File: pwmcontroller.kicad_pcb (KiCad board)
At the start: 2 copper layers, 46.2 x 53.8 mm, 19 parts, among them J1 CONN_01X04, J2 CONN_01X04, U1 WPMIx9200501S, U2 NE555

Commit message: Fix component values
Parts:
- R1: value 100K -> 1K
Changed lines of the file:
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@@
   )
   (setup
-    (last_trace_width 0.5)
+    (last_trace_width 0.25)
     (user_trace_width 0.25)
     (user_trace_width 0.5)
@@
       (effects (font (size 1 1) (thickness 0.15)))
     )
-    (fp_text value 100K (at 5.08 2.31 270) (layer F.Fab)
+    (fp_text value 1K (at 5.08 2.31 270) (layer F.Fab)
       (effects (font (size 1 1) (thickness 0.15)))
     )
@@
   (segment (start 150.114 89.408) (end 147.574 89.408) (width 1.5) (layer F.Cu) (net 10))
   (segment (start 152.52 91.814) (end 150.114 89.408) (width 1.5) (layer F.Cu) (net 10))
-  (segment (start 160.274 93.98) (end 160.274 91.948) (width 0.5) (layer B.Cu) (net 11) (status 400000))
-  (segment (start 149.98 92.082) (end 149.98 94) (width 0.5) (layer B.Cu) (net 11) (status 800000))
+  (segment (start 160.274 93.98) (end 160.274 91.948) (width 0.5) (layer B.Cu) (net 11))
+  (segment (start 149.98 92.082) (end 149.98 94) (width 0.5) (layer B.Cu) (net 11))
   (segment (start 150.876 91.186) (end 149.98 92.082) (width 0.5) (layer B.Cu) (net 11))
   (segment (start 152.794 91.186) (end 150.876 91.186) (width 0.5) (layer B.Cu) (net 11))

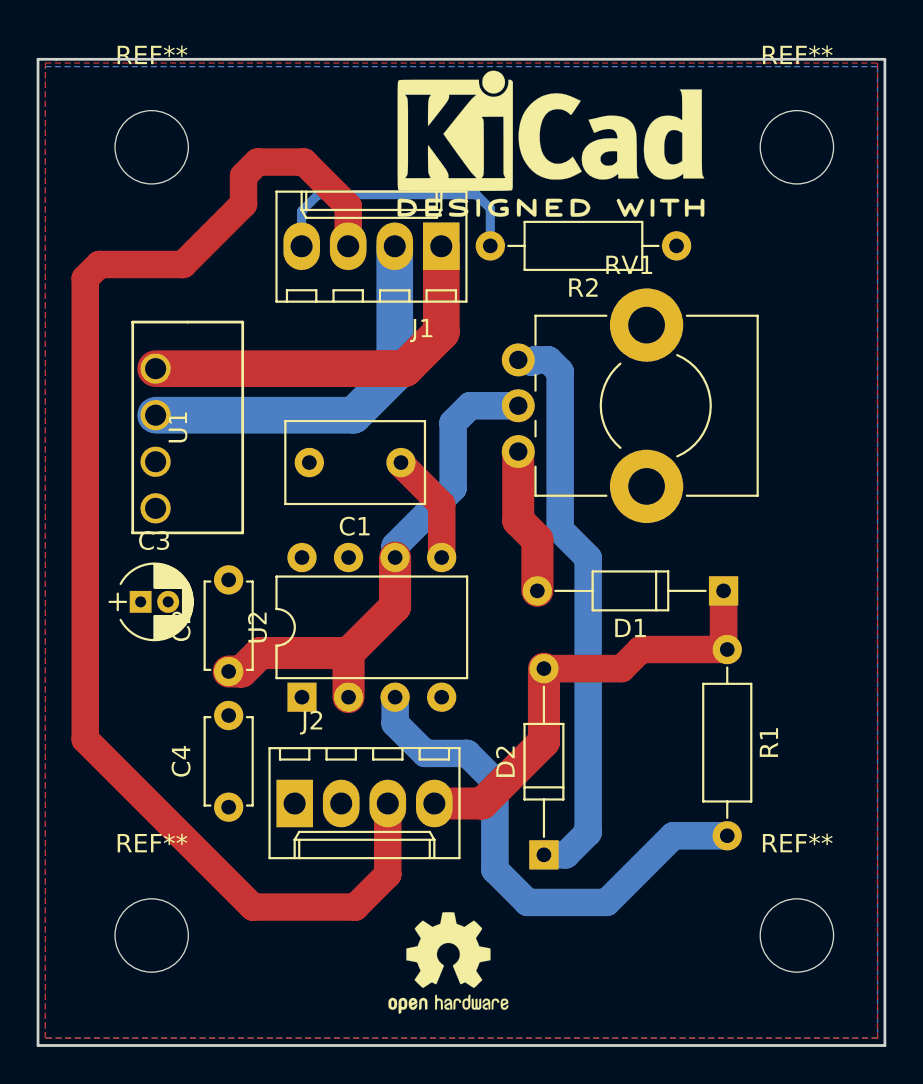
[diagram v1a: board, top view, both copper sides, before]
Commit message: Remove mounting hole silkscreen label
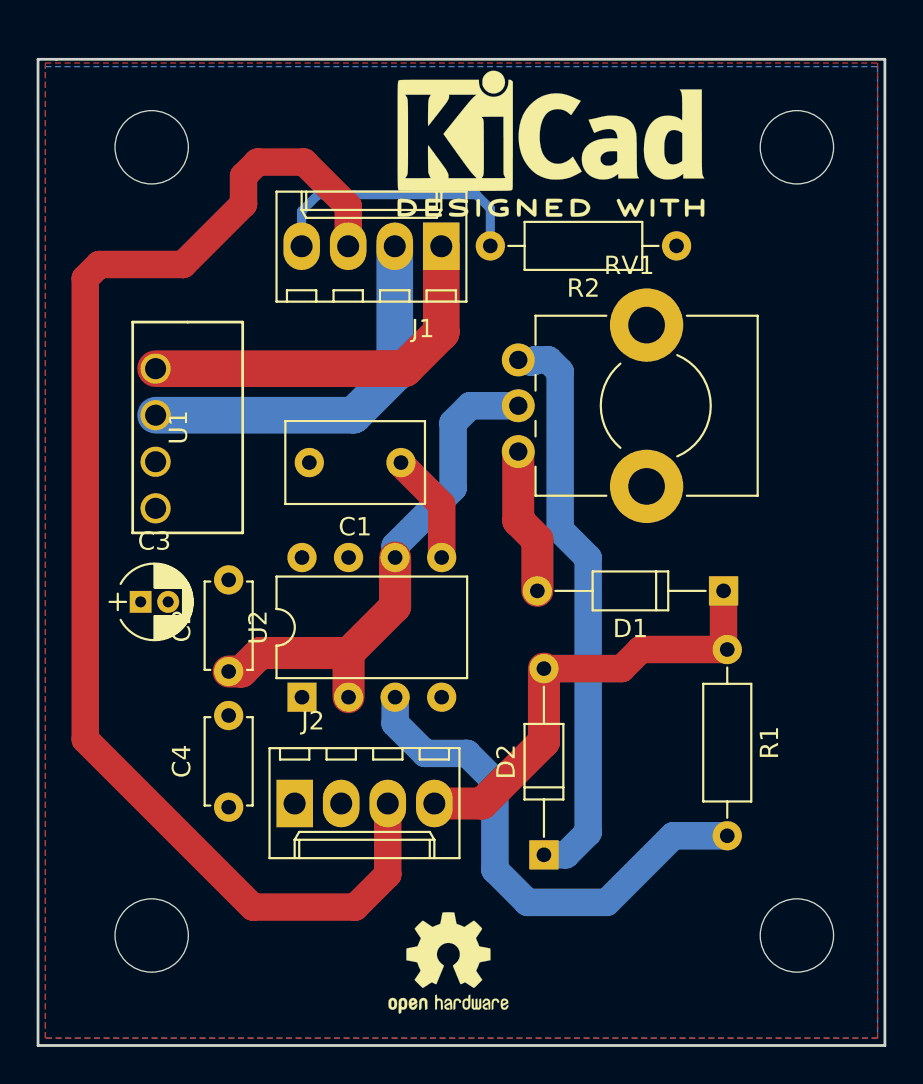
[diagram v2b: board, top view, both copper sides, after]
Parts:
- renumbered REF** to ?
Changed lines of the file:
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@@
     (links 26)
     (no_connects 0)
-    (area 135.524999 83.724999 181.875001 137.675001)
+    (area 134.385714 82.625 184.414286 137.675001)
     (thickness 1.6)
     (drawings 5)
@@
   (page A4)
   (layers
-    (0 F.Cu signal hide)
-    (31 B.Cu signal)
+    (0 F.Cu signal)
+    (31 B.Cu signal hide)
     (32 B.Adhes user)
     (33 F.Adhes user)
@@
     (descr "Mounting Hole 4mm, no annular")
     (tags "mounting hole 4mm no annular")
-    (fp_text reference REF** (at 0 -5) (layer F.SilkS)
+    (fp_text reference "" (at 0 -5) (layer F.SilkS)
       (effects (font (size 1 1) (thickness 0.15)))
     )
@@
     (descr "Mounting Hole 4mm, no annular")
     (tags "mounting hole 4mm no annular")
-    (fp_text reference REF** (at 0 -5) (layer F.SilkS)
+    (fp_text reference "" (at 0 -5) (layer F.SilkS)
       (effects (font (size 1 1) (thickness 0.15)))
     )
@@
     (descr "Mounting Hole 4mm, no annular")
     (tags "mounting hole 4mm no annular")
-    (fp_text reference REF** (at 0 -5) (layer F.SilkS)
+    (fp_text reference "" (at 0 -5) (layer F.SilkS)
       (effects (font (size 1 1) (thickness 0.15)))
     )
@@
     (descr "Mounting Hole 4mm, no annular")
     (tags "mounting hole 4mm no annular")
-    (fp_text reference REF** (at 0 -5) (layer F.SilkS)
-      (effects (font (size 1 1) (thickness 0.15)))
-    )
+    (fp_text reference "" (at 0 -5) (layer F.SilkS)
+      (effects (font (size 1 1) (thickness 0.15)))
+    )

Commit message: Shrink PCB to smaller dimensions
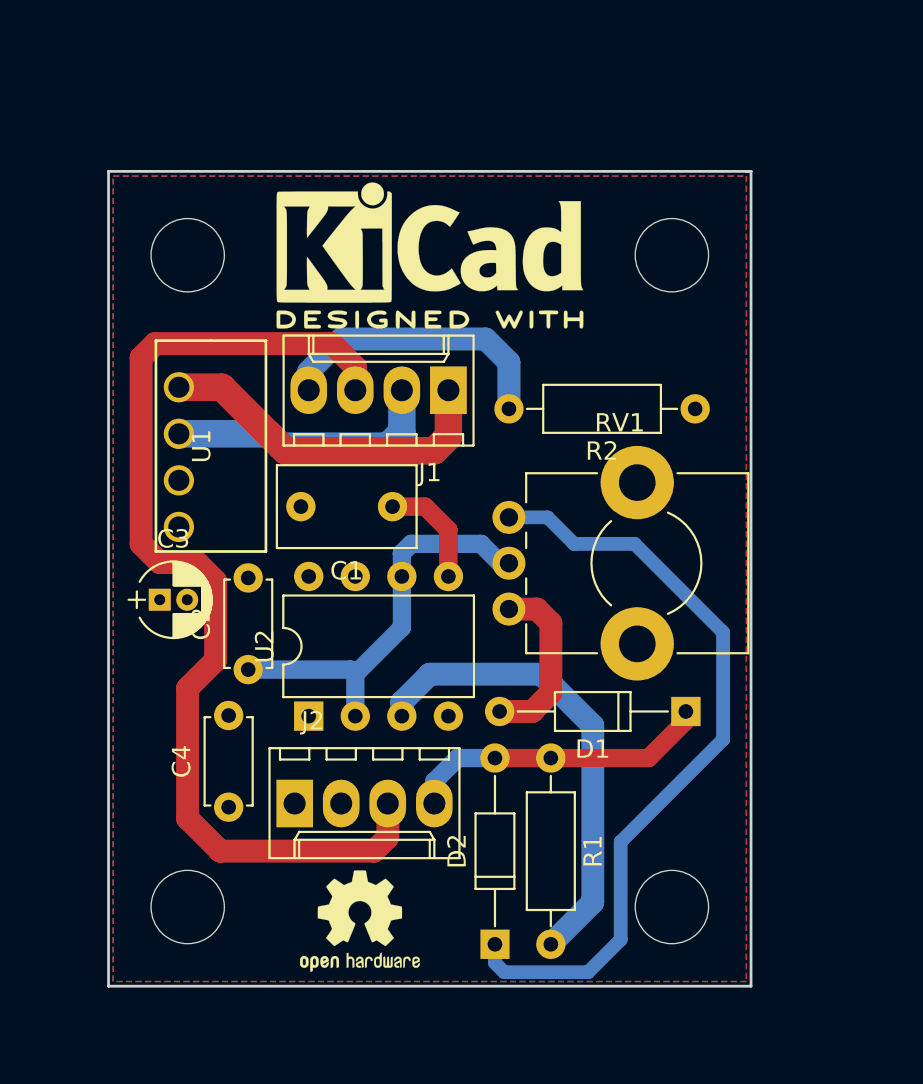
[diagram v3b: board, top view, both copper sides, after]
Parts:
- moved R1 11.3 mm to (163.6, 121.9)
- moved ? 9.01 mm to (170.2, 94.5)
- moved REF*** 8.99 mm to (157.0, 94.5)
- moved R2 8.95 mm to (171.4, 102.9)
- moved RV1 8.61 mm to (161.3, 113.8)
- moved J1 7.86 mm to (158.0, 101.9)
- moved ? 6.99 mm to (170.2, 130.0)
- moved D1 6.89 mm to (170.9, 119.4)
- moved ? 6.21 mm to (143.8, 94.5)
- moved D2 5.56 mm to (160.5, 132.1)
- moved REF*** 5.34 mm to (153.2, 130.8)
- moved ? 2.50 mm to (143.8, 130.0)
- moved C1 2.45 mm to (154.9, 108.2)
- moved U1 1.63 mm to (145.0, 104.9)
- moved U2 1.10 mm to (150.4, 119.6)
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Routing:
- net /FAN_RPM: track 71.1 -> 56.3 mm
- net Net-(D2-Pad1): track 31.3 -> 42.2 mm
- net /PWM_OUT: track 25.1 -> 16.8 mm
- net +12V: track 20.9 -> 15.0 mm
- net /TRIG: track 28.2 -> 22.4 mm
- net GNDS: track 21.1 -> 19.0 mm
- net Net-(R1-Pad2): track 27.9 -> 25.8 mm
- net Net-(D1-Pad2): track 8.03 -> 9.63 mm
- net Net-(J1-Pad4): track 14.9 -> 15.7 mm
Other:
- board size 46.2 x 53.8 mm -> 35.1 x 44.5 mm

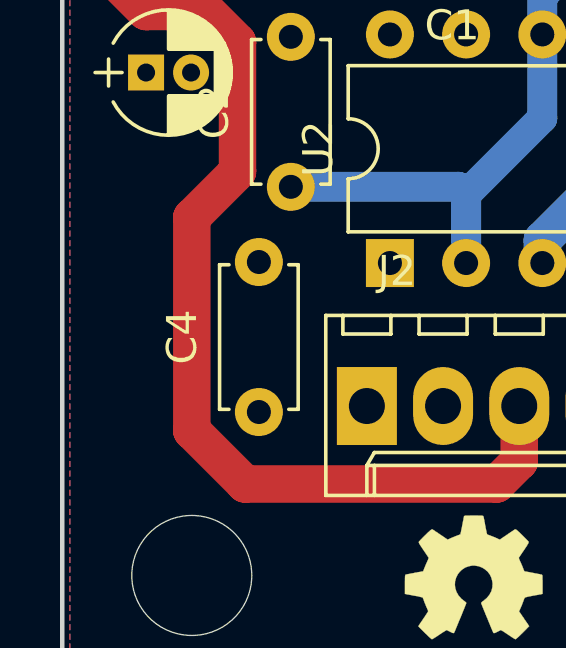
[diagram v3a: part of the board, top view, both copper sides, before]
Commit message: Add Silkscreen description on Board
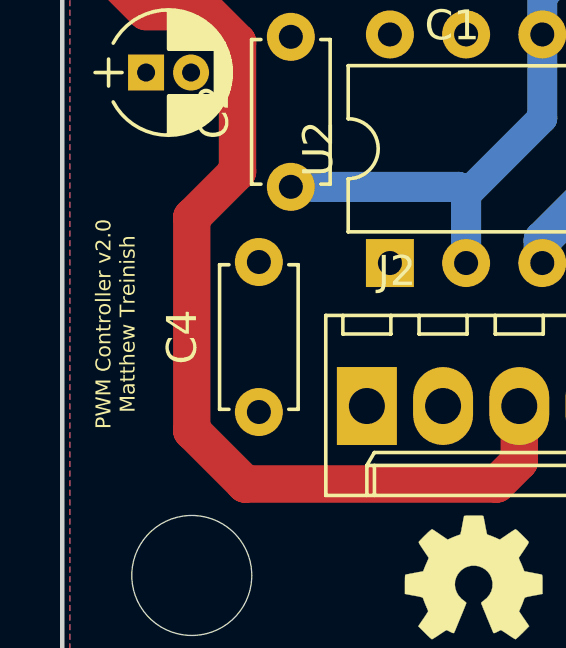
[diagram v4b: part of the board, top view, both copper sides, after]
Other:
- board text added: "PWM Controller v2.0 Matthew Treinish"
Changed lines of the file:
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@@
     (links 26)
     (no_connects 1)
-    (area 136.349714 88.513 177.594286 136.123)
+    (area 139.370999 89.840999 174.573001 134.441001)
     (thickness 1.6)
-    (drawings 5)
+    (drawings 6)
     (tracks 72)
     (zones 0)
@@
     )
   )
+  (gr_text "PWM Controller v2.0\nMatthew Treinish" (at 141.224 121.666 90) (layer F.SilkS)
+    (effects (font (size 0.5 0.5) (thickness 0.125)))
+  )
   (gr_line (start 174.498 89.916) (end 174.244 89.916) (angle 90) (layer Edge.Cuts) (width 0.15))

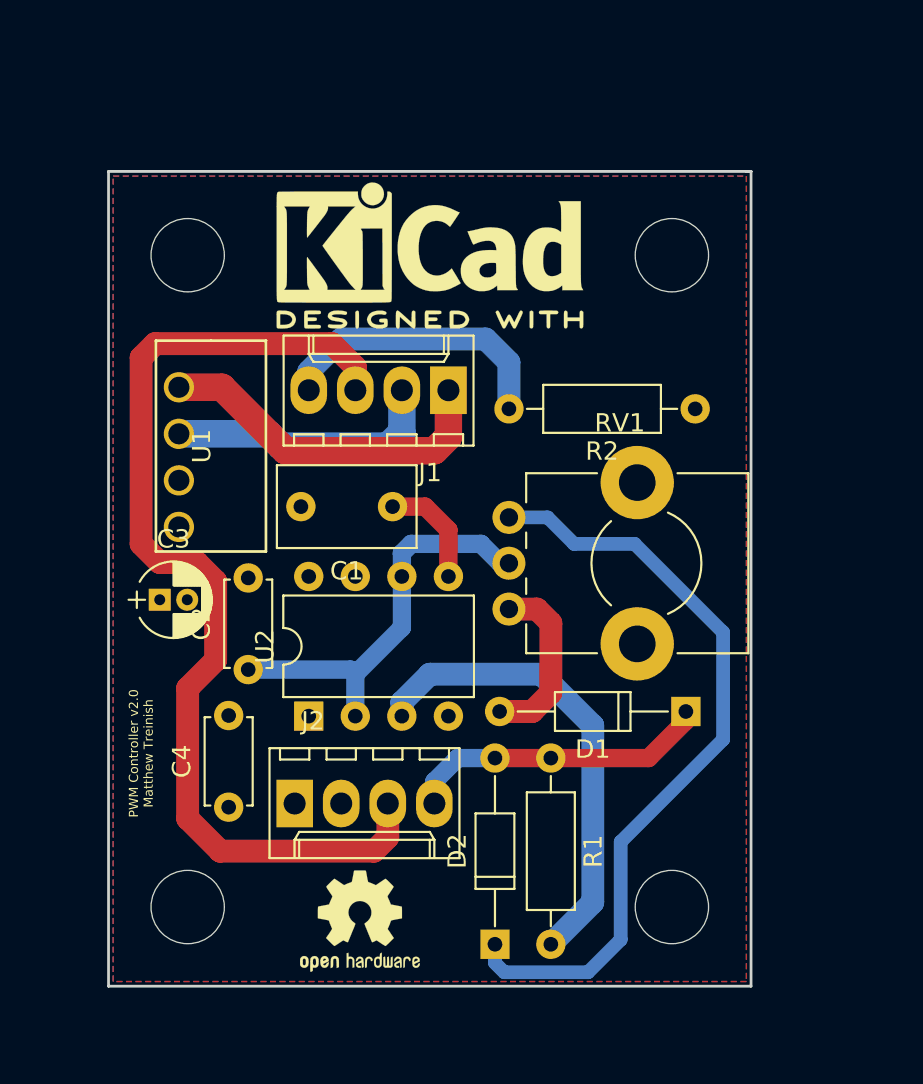
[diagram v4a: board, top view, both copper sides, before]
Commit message: Move mouting holes in slightly
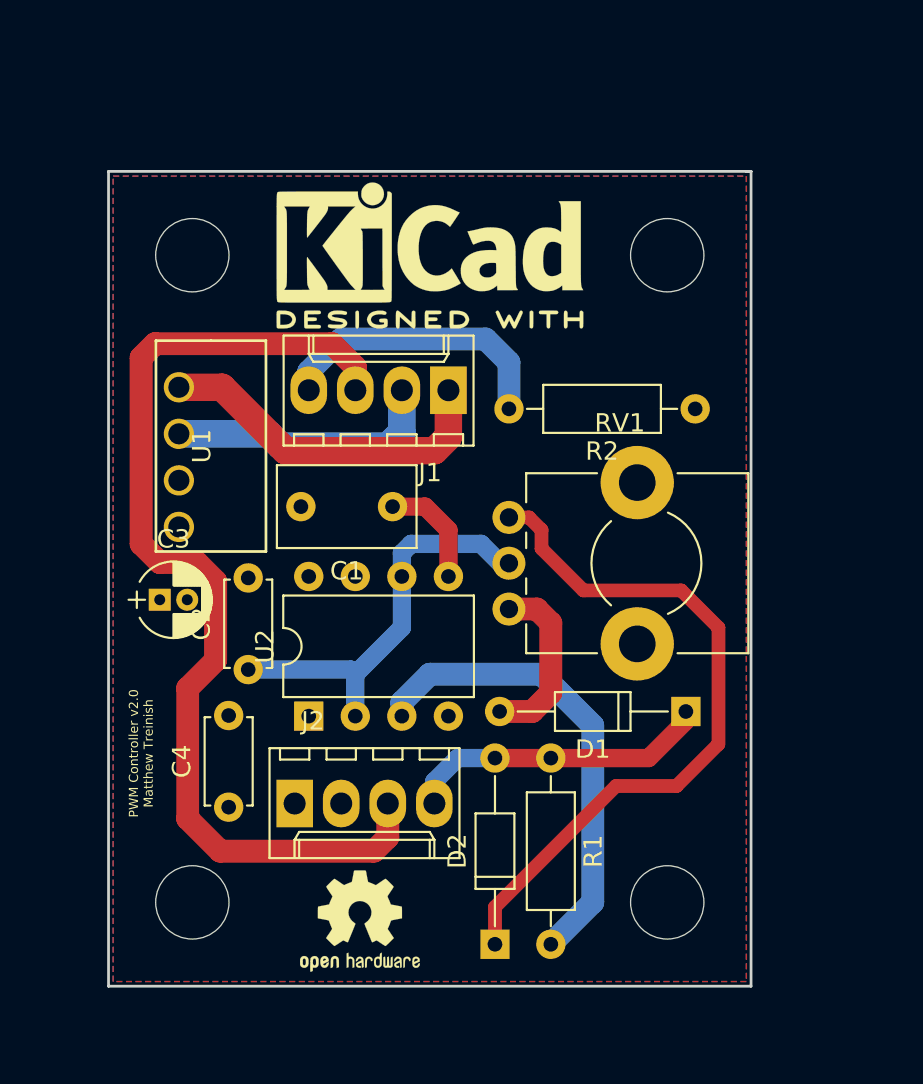
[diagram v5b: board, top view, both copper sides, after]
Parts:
- moved ? 0.36 mm to (169.9, 129.8)
- moved ? 0.36 mm to (144.0, 129.8)
- moved ? 0.25 mm to (169.9, 94.5)
- moved ? 0.25 mm to (144.0, 94.5)
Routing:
- net Net-(D2-Pad1): track 42.2 -> 38.8 mm
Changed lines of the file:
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@@
   )
   (setup
-    (last_trace_width 0.25)
+    (last_trace_width 0.75)
     (user_trace_width 0.25)
     (user_trace_width 0.5)
@@
   )
   (module Mounting_Holes:MountingHole_4mm (layer F.Cu)
-    (at 143.764 130.048)
+    (at 144.018 129.794)
     (descr "Mounting Hole 4mm, no annular")
     (tags "mounting hole 4mm no annular")
@@
   )
   (module Mounting_Holes:MountingHole_4mm (layer F.Cu)
-    (at 170.18 130.048)
+    (at 169.926 129.794)
     (descr "Mounting Hole 4mm, no annular")
     (tags "mounting hole 4mm no annular")
@@
   )
   (module Mounting_Holes:MountingHole_4mm (layer F.Cu)
-    (at 170.18 94.488)
+    (at 169.926 94.488)
     (descr "Mounting Hole 4mm, no annular")
     (tags "mounting hole 4mm no annular")
@@
   )
   (module Mounting_Holes:MountingHole_4mm (layer F.Cu)
-    (at 143.764 94.488)
+    (at 144.018 94.488)
     (descr "Mounting Hole 4mm, no annular")
     (tags "mounting hole 4mm no annular")
@@
   (segment (start 163.576 118.364) (end 163.576 114.554) (width 1.25) (layer F.Cu) (net 6))
   (segment (start 162.56 119.38) (end 163.576 118.364) (width 1.25) (layer F.Cu) (net 6))
-  (segment (start 160.528 132.08) (end 160.528 133.096) (width 0.75) (layer B.Cu) (net 7))
-  (segment (start 163.402 108.792) (end 161.29 108.792) (width 0.75) (layer B.Cu) (net 7))
-  (segment (start 164.846 110.236) (end 163.402 108.792) (width 0.75) (layer B.Cu) (net 7))
-  (segment (start 168.148 110.236) (end 164.846 110.236) (width 0.75) (layer B.Cu) (net 7))
-  (segment (start 172.974 115.062) (end 168.148 110.236) (width 0.75) (layer B.Cu) (net 7))
-  (segment (start 172.974 120.904) (end 172.974 115.062) (width 0.75) (layer B.Cu) (net 7))
-  (segment (start 167.386 126.492) (end 172.974 120.904) (width 0.75) (layer B.Cu) (net 7))
-  (segment (start 167.386 131.826) (end 167.386 126.492) (width 0.75) (layer B.Cu) (net 7))
-  (segment (start 165.608 133.604) (end 167.386 131.826) (width 0.75) (layer B.Cu) (net 7))
-  (segment (start 161.036 133.604) (end 165.608 133.604) (width 0.75) (layer B.Cu) (net 7))
-  (segment (start 160.528 133.096) (end 161.036 133.604) (width 0.75) (layer B.Cu) (net 7))
+  (segment (start 160.528 132.08) (end 160.528 130.048) (width 0.75) (layer F.Cu) (net 7) (status 400000))
+  (segment (start 162.386 108.792) (end 161.29 108.792) (width 0.75) (layer F.Cu) (net 7) (status 800000))
+  (segment (start 163.068 109.474) (end 162.386 108.792) (width 0.75) (layer F.Cu) (net 7))
+  (segment (start 163.068 110.49) (end 163.068 109.474) (width 0.75) (layer F.Cu) (net 7))
+  (segment (start 165.354 112.776) (end 163.068 110.49) (width 0.75) (layer F.Cu) (net 7))
+  (segment (start 170.688 112.776) (end 165.354 112.776) (width 0.75) (layer F.Cu) (net 7))
+  (segment (start 172.72 114.808) (end 170.688 112.776) (width 0.75) (layer F.Cu) (net 7))
+  (segment (start 172.72 121.158) (end 172.72 114.808) (width 0.75) (layer F.Cu) (net 7))
+  (segment (start 170.434 123.444) (end 172.72 121.158) (width 0.75) (layer F.Cu) (net 7))
+  (segment (start 167.132 123.444) (end 170.434 123.444) (width 0.75) (layer F.Cu) (net 7))
+  (segment (start 160.528 130.048) (end 167.132 123.444) (width 0.75) (layer F.Cu) (net 7))
   (segment (start 143.284 101.692) (end 145.634 101.692) (width 1.5) (layer F.Cu) (net 8))
   (segment (start 157.988 104.394) (end 157.988 101.854) (width 1.5) (layer F.Cu) (net 8))

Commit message: Remove extra labels
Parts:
- ? (x4): value MountingHole_4mm -> (none)
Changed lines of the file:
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@@
     (links 26)
     (no_connects 1)
-    (area 139.370999 89.840999 174.573001 134.441001)
+    (area 136.603714 88.513 177.340286 135.869)
     (thickness 1.6)
     (drawings 6)
@@
   )
   (setup
-    (last_trace_width 0.75)
+    (last_trace_width 0.25)
     (user_trace_width 0.25)
     (user_trace_width 0.5)
@@
       (effects (font (size 1 1) (thickness 0.15)))
     )
-    (fp_text value MountingHole_4mm (at 0 5) (layer F.Fab)
+    (fp_text value "" (at 0 5) (layer F.Fab)
       (effects (font (size 1 1) (thickness 0.15)))
     )
@@
       (effects (font (size 1 1) (thickness 0.15)))
     )
-    (fp_text value MountingHole_4mm (at 0 5) (layer F.Fab)
+    (fp_text value "" (at 0 5) (layer F.Fab)
       (effects (font (size 1 1) (thickness 0.15)))
     )
@@
       (effects (font (size 1 1) (thickness 0.15)))
     )
-    (fp_text value MountingHole_4mm (at 0 5) (layer F.Fab)
+    (fp_text value "" (at 0 5) (layer F.Fab)
       (effects (font (size 1 1) (thickness 0.15)))
     )
@@
       (effects (font (size 1 1) (thickness 0.15)))
     )
-    (fp_text value MountingHole_4mm (at 0 5) (layer F.Fab)
+    (fp_text value "" (at 0 5) (layer F.Fab)
       (effects (font (size 1 1) (thickness 0.15)))
     )
@@
   (segment (start 163.576 118.364) (end 163.576 114.554) (width 1.25) (layer F.Cu) (net 6))
   (segment (start 162.56 119.38) (end 163.576 118.364) (width 1.25) (layer F.Cu) (net 6))
-  (segment (start 160.528 132.08) (end 160.528 130.048) (width 0.75) (layer F.Cu) (net 7) (status 400000))
-  (segment (start 162.386 108.792) (end 161.29 108.792) (width 0.75) (layer F.Cu) (net 7) (status 800000))
+  (segment (start 160.528 132.08) (end 160.528 130.048) (width 0.75) (layer F.Cu) (net 7))
+  (segment (start 162.386 108.792) (end 161.29 108.792) (width 0.75) (layer F.Cu) (net 7))
   (segment (start 163.068 109.474) (end 162.386 108.792) (width 0.75) (layer F.Cu) (net 7))
   (segment (start 163.068 110.49) (end 163.068 109.474) (width 0.75) (layer F.Cu) (net 7))
